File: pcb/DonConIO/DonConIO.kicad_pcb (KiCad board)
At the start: 2 copper layers, 130.8 x 58.4 mm, 100 parts, among them J1 Ka Left, J2 Don Left, J3 Don Right, J4 Ka Right, J5 Pad, J6 Conn_01x07, J7 Conn_01x07, J8 Conn_02x04_Top_Bottom, J9 Conn_01x03, U1 TL072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

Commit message: Change some resistor values to improve sensitivity
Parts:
- D12, D18, D24, D6: value 4.7V 5mA -> 3.3V 20mA
- R14, R23, R32, R5: value 3.3k -> 0
- R15, R24, R33, R6: value 1.8k -> 5.1k
- R18, R27, R36, R9: value 22 -> 300
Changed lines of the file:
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@@
       (effects (font (size 1 1) (thickness 0.15)))
     )
-    (fp_text value "3.3k" (at 3.81 2.37 -180) (layer "F.Fab")
+    (fp_text value "0" (at 3.81 2.37 -180) (layer "F.Fab")
       (effects (font (size 1 1) (thickness 0.15)))
     )
@@
       (effects (font (size 1 1) (thickness 0.15)))
     )
-    (fp_text value "1.8k" (at 3.81 2.37 -90) (layer "F.Fab")
+    (fp_text value "5.1k" (at 3.81 2.37 -90) (layer "F.Fab")
       (effects (font (size 1 1) (thickness 0.15)))
     )
@@
       (effects (font (size 1 1) (thickness 0.15)))
     )
-    (fp_text value "1.8k" (at 3.81 2.37 -90) (layer "F.Fab")
+    (fp_text value "5.1k" (at 3.81 2.37 -90) (layer "F.Fab")
       (effects (font (size 1 1) (thickness 0.15)))
     )
@@
       (effects (font (size 1 1) (thickness 0.15)))
     )
-    (fp_text value "22" (at 3.81 2.37) (layer "F.Fab")
+    (fp_text value "300" (at 3.81 2.37) (layer "F.Fab")
       (effects (font (size 1 1) (thickness 0.15)))
     )
@@
       (effects (font (size 1 1) (thickness 0.15)))
     )
-    (fp_text value "1.8k" (at 3.81 2.37 -90) (layer "F.Fab")
+    (fp_text value "5.1k" (at 3.81 2.37 -90) (layer "F.Fab")
       (effects (font (size 1 1) (thickness 0.15)))
     )
@@
       (effects (font (size 1 1) (thickness 0.15)))
     )
-    (fp_text value "4.7V 5mA" (at 3.81 2.12 -90) (layer "F.Fab")
+    (fp_text value "3.3V 20mA" (at 3.81 2.12 -90) (layer "F.Fab")
       (effects (font (size 1 1) (thickness 0.15)))
     )
@@
       (effects (font (size 1 1) (thickness 0.15)))
     )
-    (fp_text value "4.7V 5mA" (at 3.81 2.12 -90) (layer "F.Fab")
+    (fp_text value "3.3V 20mA" (at 3.81 2.12 -90) (layer "F.Fab")
       (effects (font (size 1 1) (thickness 0.15)))
     )
@@
       (effects (font (size 1 1) (thickness 0.15)))
     )
-    (fp_text value "22" (at 3.81 2.37) (layer "F.Fab")
+    (fp_text value "300" (at 3.81 2.37) (layer "F.Fab")
       (effects (font (size 1 1) (thickness 0.15)))
     )
@@
       (effects (font (size 1 1) (thickness 0.15)))
     )
-    (fp_text value "4.7V 5mA" (at 3.81 2.12 -90) (layer "F.Fab")
+    (fp_text value "3.3V 20mA" (at 3.81 2.12 -90) (layer "F.Fab")
       (effects (font (size 1 1) (thickness 0.15)))
     )
@@
       (effects (font (size 1 1) (thickness 0.15)))
     )
-    (fp_text value "1.8k" (at 3.81 2.37 -90) (layer "F.Fab")
+    (fp_text value "5.1k" (at 3.81 2.37 -90) (layer "F.Fab")
       (effects (font (size 1 1) (thickness 0.15)))
     )
@@
       (effects (font (size 1 1) (thickness 0.15)))
     )
-    (fp_text value "22" (at 3.81 2.37) (layer "F.Fab")
+    (fp_text value "300" (at 3.81 2.37) (layer "F.Fab")
       (effects (font (size 1 1) (thickness 0.15)))
     )
@@
       (effects (font (size 1 1) (thickness 0.15)))
     )
-    (fp_text value "4.7V 5mA" (at 3.81 2.12 -90) (layer "F.Fab")
+    (fp_text value "3.3V 20mA" (at 3.81 2.12 -90) (layer "F.Fab")
       (effects (font (size 1 1) (thickness 0.15)))
     )
@@
       (effects (font (size 1 1) (thickness 0.15)))
     )
-    (fp_text value "3.3k" (at 4.064 2.54 -180) (layer "F.Fab")
+    (fp_text value "0" (at 4.064 2.54 -180) (layer "F.Fab")
       (effects (font (size 1 1) (thickness 0.15)))
     )
@@
       (effects (font (size 1 1) (thickness 0.15)))
     )
-    (fp_text value "3.3k" (at 3.81 2.37 -180) (layer "F.Fab")
+    (fp_text value "0" (at 3.81 2.37 -180) (layer "F.Fab")
       (effects (font (size 1 1) (thickness 0.15)))
     )
@@
       (effects (font (size 1 1) (thickness 0.15)))
     )
-    (fp_text value "3.3k" (at 3.81 2.37 -180) (layer "F.Fab")
+    (fp_text value "0" (at 3.81 2.37 -180) (layer "F.Fab")
       (effects (font (size 1 1) (thickness 0.15)))
     )
@@
       (effects (font (size 1 1) (thickness 0.15)))
     )
-    (fp_text value "22" (at 3.81 2.37) (layer "F.Fab")
+    (fp_text value "300" (at 3.81 2.37) (layer "F.Fab")
       (effects (font (size 1 1) (thickness 0.15)))
     )

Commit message: Add external ADC to DonConIO PCB
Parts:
- removed J8: Conn_02x04_Top_Bottom, Connector_PinHeader_2.54mm:PinHeader_2x04_P2.54mm_Vertical
- added C20: 0.1uF, Capacitor_SMD:C_0805_2012Metric_Pad1.18x1.45mm_HandSolder, F.Cu at (149.2, 91.8)
- added C21: 10uF, Capacitor_SMD:C_0805_2012Metric_Pad1.18x1.45mm_HandSolder, F.Cu at (154.9, 91.8)
- added C22: 0.1uF, Capacitor_SMD:C_0805_2012Metric_Pad1.18x1.45mm_HandSolder, F.Cu at (149.2, 96.8)
- added C23: 10uF, Capacitor_SMD:C_0805_2012Metric_Pad1.18x1.45mm_HandSolder, F.Cu at (156.8, 70.9)
- added C24: 0.1uF, Capacitor_SMD:C_0805_2012Metric_Pad1.18x1.45mm_HandSolder, F.Cu at (155.2, 84.5)
- added C25: 0.1uF, Capacitor_SMD:C_0805_2012Metric_Pad1.18x1.45mm_HandSolder, F.Cu at (151.0, 84.5)
- added JP1: Ka Left, Jumper:SolderJumper-3_P2.0mm_Open_TrianglePad1.0x1.5mm_NumberLabels, F.Cu at (101.0, 74.3)
- added JP2: Don Left, Jumper:SolderJumper-3_P2.0mm_Open_TrianglePad1.0x1.5mm_NumberLabels, F.Cu at (125.7, 74.3)
- added JP3: Ka Left, Jumper:SolderJumper-3_P2.0mm_Open_TrianglePad1.0x1.5mm_NumberLabels, F.Cu at (170.8, 74.2)
- added JP4: Ka Left, Jumper:SolderJumper-3_P2.0mm_Open_TrianglePad1.0x1.5mm_NumberLabels, F.Cu at (195.6, 74.2)
- added R37: 10k, Resistor_SMD:R_0805_2012Metric_Pad1.20x1.40mm_HandSolder, F.Cu at (150.9, 73.0)
- added REF02: Donchan-Logo_6.3mm_Silkscreen, CustomLogos:Donchan-Logo_6.3mm_Silkscreen, F.Cu at (188.0, 120.0)
- added U5: MCP3204, Package_SO:SOIC-14_3.9x8.7mm_P1.27mm, F.Cu at (154.9, 97.9)
- added U6: MCP1541-TT, Package_TO_SOT_SMD:SOT-23, F.Cu at (152.1, 91.9)
- added U7: TXB0104D, Package_SO:SOIC-14_3.9x8.7mm_P1.27mm, F.Cu at (153.0, 78.7)
- D12, D18, D24: value 3.3V 20mA -> 4.3V
- D6: value 3.3V 20mA -> 4.1V
- J6: value Conn_01x07 -> MCU1
- J7: value Conn_01x07 -> MCU2
- J9: value Conn_01x03 -> Power 12V
- moved REF01 67.4 mm to (113.0, 71.1)
- moved REF** 62.5 mm to (90.8, 109.9), turned to 90 degrees
- moved J9 28.9 mm to (144.8, 119.4), turned to 180 degrees
- moved C18 28.0 mm to (158.6, 120.5), turned to 90 degrees
- moved REF02 27.9 mm to (118.1, 120.0)
- moved C19 18.0 mm to (158.6, 115.0), turned to 90 degrees
- moved C17 9.99 mm to (158.6, 106.7), turned to -90 degrees
- moved PS1 1.54 mm to (153.7, 106.7), turned to 0 degrees
- moved D24 0.33 mm to (196.2, 80.3), turned to 180 degrees
- moved D18 0.30 mm to (171.4, 80.3), turned to 180 degrees
- moved D6 0.25 mm to (101.6, 80.2), turned to 180 degrees
- turned D12 to 180 degrees
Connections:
- net Don_Left renamed Don_Left_IN
- net Don_Right renamed Don_Right_IN
- net Ka_Left renamed Ka_Left_IN
- net Ka_Right renamed Ka_Right_IN
- J6 pad 1: Net-(D6-K) -> Ka_Left_DIRECT
- J6 pad 2: Net-(D12-K) -> Don_Left_DIRECT
- J6 pad 3: Net-(D18-K) -> Don_Right_DIRECT
- J6 pad 4: Net-(D24-K) -> Ka_Right_DIRECT
- J6 pad 7: GPIO 0 -> SPI OE
- J7 pad 4: GPIO 3 -> SPI MOSI
- J7 pad 5: GPIO 4 -> SPI MISO
- J7 pad 6: GPIO 2 -> SPI SCLK
- J7 pad 7: GPIO 1 -> SPI nCS
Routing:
- net Ka_Left_ADC: track 0.00 -> 84.9 mm, vias 0 -> 2
- net Ka_Right_DIRECT: track 0.00 -> 80.5 mm
- net Ka_Right_ADC: track 0.00 -> 70.2 mm, vias 0 -> 2
- net Net-(D24-K): track 80.3 -> 11.8 mm
- net Don_Left_ADC: track 0.00 -> 61.3 mm, vias 0 -> 2
- net Don_Right_DIRECT: track 0.00 -> 56.7 mm
- net Ka_Left_DIRECT: track 0.00 -> 44.8 mm
- net Don_Right_ADC: track 0.00 -> 44.5 mm, vias 0 -> 2
- net Net-(D18-K): track 53.8 -> 11.9 mm
- net Net-(D6-K): track 52.5 -> 11.4 mm
- net GPIO 1: track 24.4 -> 0.00 mm
- net Net-(U5-Din): track 0.00 -> 23.8 mm, vias 0 -> 2
- net Net-(U5-Dout): track 0.00 -> 21.9 mm, vias 0 -> 2
- net +5V: track 54.9 -> 76.1 mm, vias 0 -> 5
- net GPIO 0: track 20.7 -> 0.00 mm
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- added copper zone on B.Cu, net GND
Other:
- board text removed: "3V3"
- board text removed: "5V"
- board text removed: "GPIO 0"
- board text removed: "GPIO 1"
- board text removed: "GPIO 2"
- board text removed: "GPIO 3"
- board text removed: "GPIO 4"

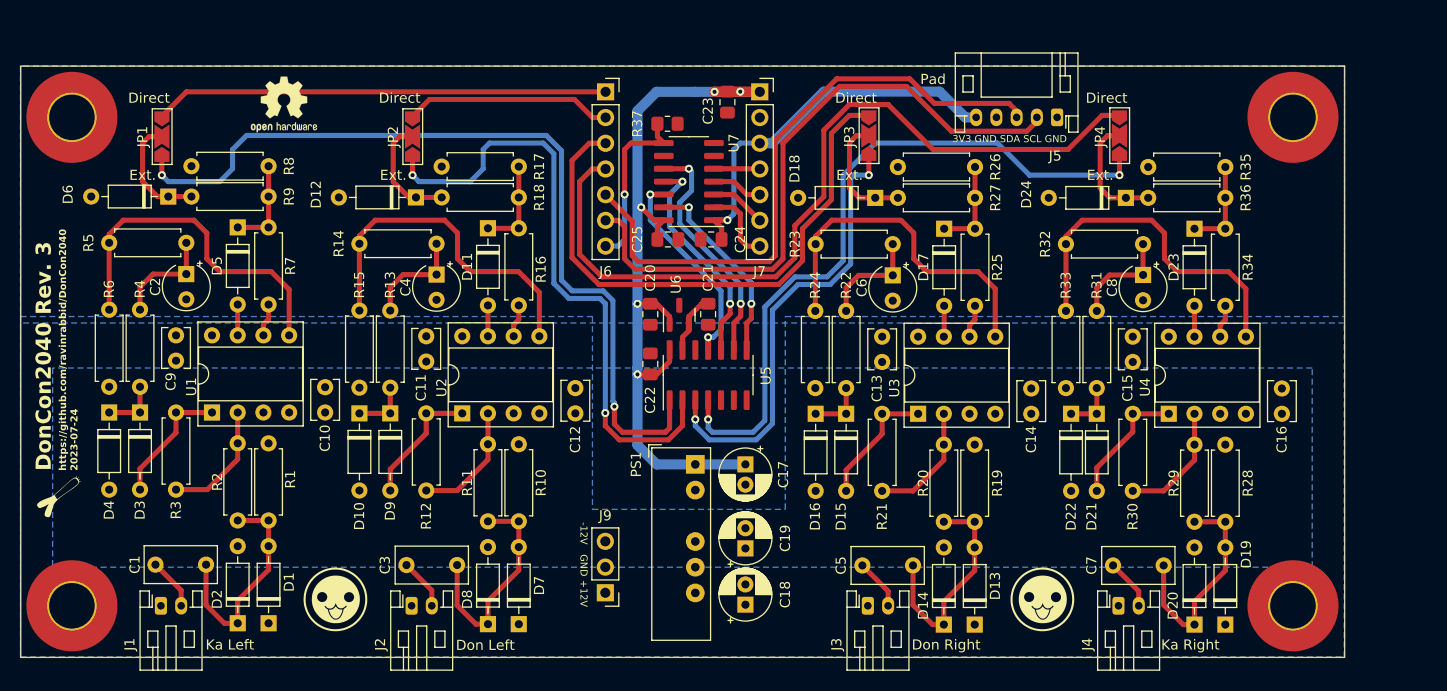
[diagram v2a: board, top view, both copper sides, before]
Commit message: Add missing level shifter to IO board
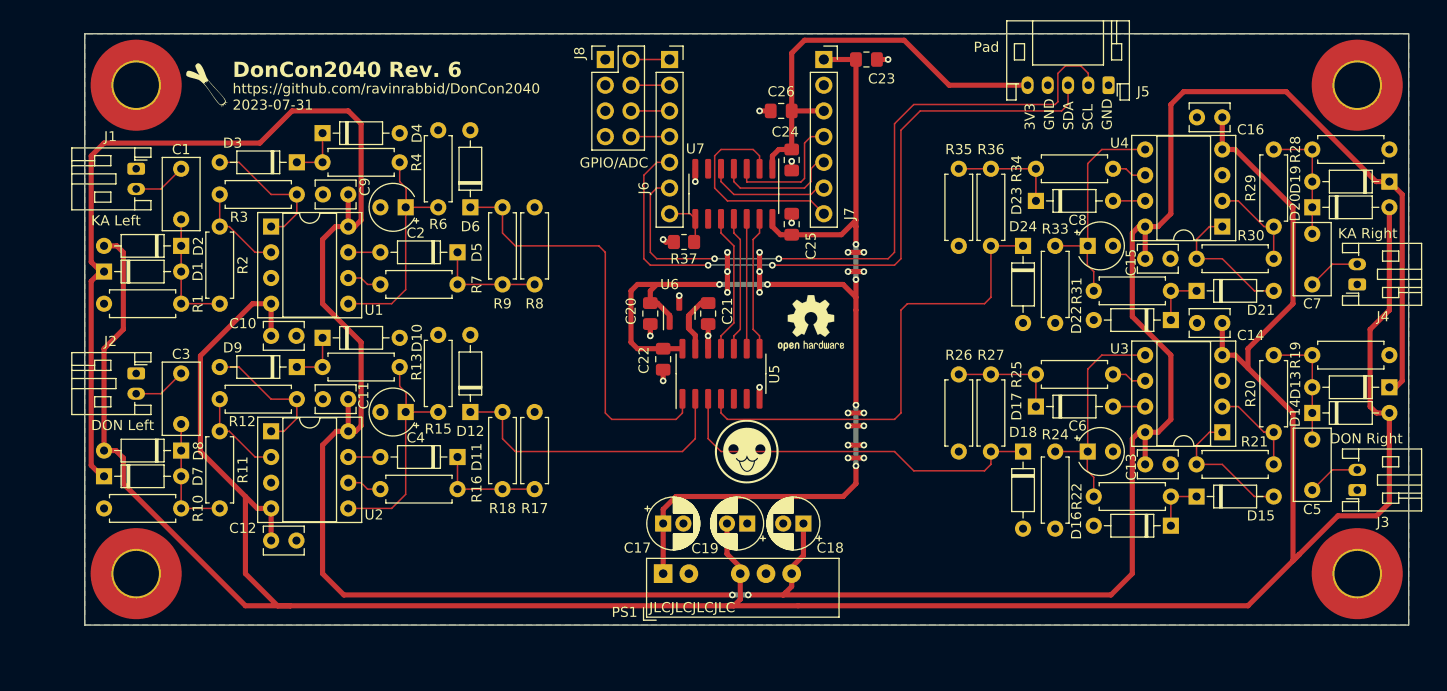
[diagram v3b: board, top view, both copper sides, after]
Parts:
- removed J9: Power 12V, Connector_PinHeader_2.54mm:PinHeader_1x03_P2.54mm_Vertical
- removed JP1, JP3, JP4: Ka Left, Jumper:SolderJumper-3_P2.0mm_Open_TrianglePad1.0x1.5mm_NumberLabels
- removed JP2: Don Left, Jumper:SolderJumper-3_P2.0mm_Open_TrianglePad1.0x1.5mm_NumberLabels
- removed R14, R23, R32, R5: 0, Resistor_THT:R_Axial_DIN0207_L6.3mm_D2.5mm_P7.62mm_Horizontal
- removed the REF02 at (188.0, 120.0)
- added C26: 10uF, Capacitor_SMD:C_0805_2012Metric_Pad1.18x1.45mm_HandSolder, F.Cu at (162.2, 71.8)
- added J8: GPIO/ADC, Connector_PinHeader_2.54mm:PinHeader_2x04_P2.54mm_Vertical, F.Cu at (144.8, 66.7)
- moved REF01 56.4 mm to (165.1, 92.7)
- moved J3 49.7 mm to (219.1, 109.2), turned to 90 degrees
- moved D13 47.2 mm to (222.2, 99.1), turned to 180 degrees
- moved D19 46.7 mm to (222.2, 78.7), turned to 180 degrees
- moved C5 45.1 mm to (214.6, 109.2), turned to 90 degrees
- moved D7 43.5 mm to (95.2, 107.9), turned to 0 degrees
- moved J1 43.2 mm to (98.4, 77.5), turned to -90 degrees
- moved REF** 43.2 mm to (105.4, 69.2), turned to 0 degrees
- moved REF02 43.2 mm to (158.8, 105.4)
- moved D20 42.8 mm to (214.6, 81.3), turned to 0 degrees
- moved D14 42.0 mm to (214.6, 101.6), turned to 0 degrees
- moved R6 41.2 mm to (128.3, 73.7), turned to -90 degrees
- moved J4 39.6 mm to (219.1, 88.9), turned to 90 degrees
- moved C1 39.2 mm to (102.9, 77.5), turned to -90 degrees
- moved R21 38.8 mm to (210.8, 106.7), turned to 180 degrees
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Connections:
- C2 pad 1: Net-(C2-Pad1) -> Net-(U1B-+)
- C4 pad 1: Net-(C4-Pad1) -> Net-(U2B-+)
- C6 pad 1: Net-(C6-Pad1) -> Net-(U3B-+)
- C8 pad 1: Net-(C8-Pad1) -> Net-(U4B-+)
- D12 pad 1: Net-(D12-K) -> Don_Left_ADC
- D18 pad 1: Net-(D18-K) -> Don_Right_ADC
- D24 pad 1: Net-(D24-K) -> Ka_Right_ADC
- D6 pad 1: Net-(D6-K) -> Ka_Left_ADC
- J6 pad 1: Ka_Left_DIRECT -> Net-(J6-Pin_1)
- J6 pad 2: Don_Left_DIRECT -> Net-(J6-Pin_2)
- J6 pad 3: Don_Right_DIRECT -> Net-(J6-Pin_3)
- J6 pad 4: Ka_Right_DIRECT -> Net-(J6-Pin_4)
- R13 pad 2: Net-(C4-Pad1) -> Net-(U2B-+)
- R18 pad 1: Net-(D12-K) -> Don_Left_ADC
- R22 pad 2: Net-(C6-Pad1) -> Net-(U3B-+)
- R27 pad 1: Net-(D18-K) -> Don_Right_ADC
- R31 pad 2: Net-(C8-Pad1) -> Net-(U4B-+)
- R36 pad 1: Net-(D24-K) -> Ka_Right_ADC
- R4 pad 2: Net-(C2-Pad1) -> Net-(U1B-+)
- R9 pad 1: Net-(D6-K) -> Ka_Left_ADC
- U7 pad 10: Net-(U5-Din) -> Net-(U5-CLK)
- U7 pad 12: Net-(U5-CLK) -> Net-(U5-Din)
- U7 pad 3: SPI SCLK -> SPI MOSI
- U7 pad 5: SPI MOSI -> SPI SCLK
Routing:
- net +12V: track 0.00 -> 317.1 mm, vias 0 -> 2
- net -12V: track 0.00 -> 308.6 mm
- net Ka_Right_DIRECT: track 80.5 -> 0.00 mm
- net Don_Right_DIRECT: track 56.7 -> 0.00 mm
- net Ka_Left_DIRECT: track 44.8 -> 0.00 mm
- net +5V: track 76.1 -> 120.2 mm, vias 5 -> 6
- net Ka_Left_ADC: track 84.9 -> 42.1 mm, vias 2 -> 0
- net Don_Left_ADC: track 61.3 -> 29.9 mm, vias 2 -> 0
- net GND: track 0.00 -> 30.4 mm, vias 0 -> 29
- net Ka_Right_ADC: track 70.2 -> 47.5 mm, vias 2 -> 0
- net Don_Left_DIRECT: track 20.5 -> 0.00 mm
- net SPI nCS: track 7.54 -> 21.3 mm
- net Net-(U4B-+): track 34.8 -> 22.3 mm
- net Net-(U3B-+): track 34.8 -> 22.3 mm
- net Net-(U1B-+): track 34.7 -> 22.3 mm
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- removed copper zone on B.Cu, net +12V
- removed copper zone on B.Cu, net -12V
- removed copper zone on F.Cu, net GND
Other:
- board text added: "3V3"
- board text added: "DON Left"
- board text added: "DON Right"
- board text added: "GPIO/ADC"
- board text added: "JLCJLCJLCJLC"
- board text added: "KA Left"
- board text added: "KA Right"
- board text added: "SCL"
- board text added: "SDA"
- board text removed: "+12V"
- board text removed: "-12V"
- board text removed: "3V3 GND SDA SCL GND"
- board text removed: "Don Left"
- board text removed: "Don Right"
- board text removed: "Ka Left"
- board text removed: "Ka Right"
